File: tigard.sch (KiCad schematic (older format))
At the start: 87 parts, among them J1 USB_C_Receptacle_USB2.0, J2 JTAG, J3 UART, J4 SPI, J5 SWD, J6 I2C, Q1 BSH103, SW1 SW_DP4T, SW2 SW_DPDT, U1 AP7365-18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

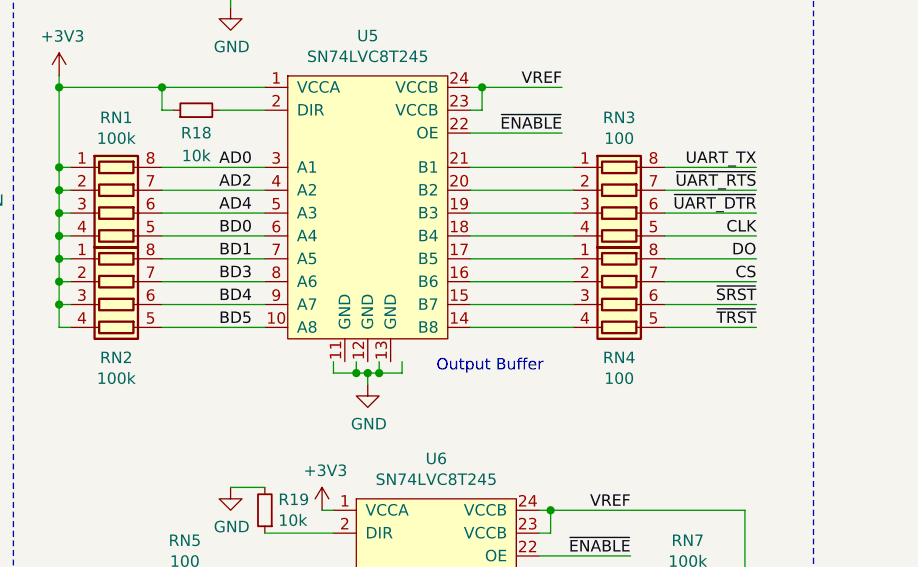
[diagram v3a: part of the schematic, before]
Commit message: Revise design to use cheaper TSSOP buffer footprint
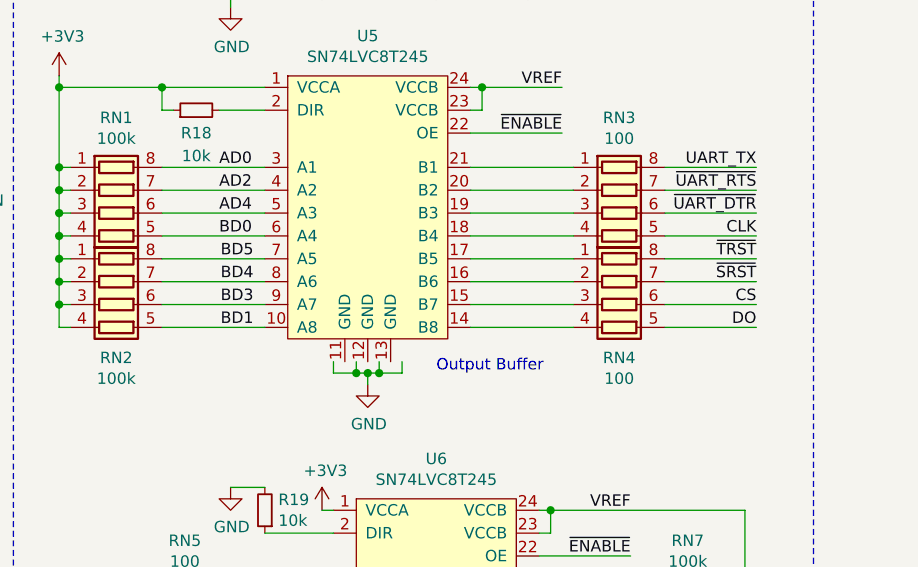
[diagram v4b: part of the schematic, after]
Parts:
- U5, U6: footprint tigard:Texas_VQFN-RHL-24_ThermalVias -> Package_SO:TSSOP-24_4.4x7.8mm_P0.65mm
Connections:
- net BD1: now also RN2.5 (R4.2), U5.10 (A8); no longer RN2.8 (R1.2), U5.7 (A5)
- net BD3: now also RN2.6 (R3.2), U5.9 (A7); no longer RN2.7 (R2.2), U5.8 (A6)
- net BD4: now also RN2.7 (R2.2), U5.8 (A6); no longer RN2.6 (R3.2), U5.9 (A7)
- net BD5: now also RN2.8 (R1.2), U5.7 (A5); no longer RN2.5 (R4.2), U5.10 (A8)
- net CS: now also RN4.6 (R3.2); no longer RN4.7 (R2.2)
- net DO: now also RN4.5 (R4.2); no longer RN4.8 (R1.2)
- net ~SRST: now also RN4.7 (R2.2); no longer RN4.6 (R3.2)
- net ~TRST: now also RN4.8 (R1.2); no longer RN4.5 (R4.2)
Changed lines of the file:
@@
 Wire Notes Line
 	4800 3050 4800 11150
-$Comp
-L tigard:SN74LVC8T245 U5
-U 1 1 5FA83347
-P 6350 5750
-F 0 "U5" H 6350 6625 50  0000 C CNN
-F 1 "SN74LVC8T245" H 6350 6534 50  0000 C CNN
-F 2 "tigard:Texas_VQFN-RHL-24_ThermalVias" H 6350 5850 50  0001 C CNN
-F 3 "" H 6350 5850 50  0001 C CNN
-F 4 "SN74LVC8T245RHLR" H 6350 5750 50  0001 C CNN "P/N"
-F 5 "C350563" H 6350 5750 50  0001 C CNN "LCSC"
-F 6 "ic-sn74lvc8t245" H 6350 5750 50  0001 C CNN "Key"
-	1    6350 5750
-	1    0    0    -1
-$EndComp
 Text Label 7200 5300 2    50   ~ 0
 ~ENABLE
@@
 Wire Wire Line
 	5450 5750 5900 5750
-Wire Wire Line
-	5450 5850 5900 5850
-Wire Wire Line
-	5450 5950 5900 5950
-Wire Wire Line
-	5450 6050 5900 6050
-Wire Wire Line
-	5450 6150 5900 6150
 $Comp
 L Device:R_Small R18
@@
 Wire Wire Line
 	5700 5200 5900 5200
-Text Label 5700 5450 0    50   ~ 0
-AD0
-Text Label 5700 5550 0    50   ~ 0
-AD2
-Text Label 5700 5650 0    50   ~ 0
-AD4
-Text Label 5700 5750 0    50   ~ 0
-BD0
-Text Label 5700 5850 0    50   ~ 0
-BD1
-Text Label 5700 5950 0    50   ~ 0
-BD3
-Text Label 5700 6050 0    50   ~ 0
-BD4
-Text Label 5700 6150 0    50   ~ 0
-BD5
-Text Label 8050 5450 2    50   ~ 0
-UART_TX
-Text Label 8050 5550 2    50   ~ 0
-~UART_RTS
-Text Label 8050 5650 2    50   ~ 0
-~UART_DTR
-Text Label 8050 5750 2    50   ~ 0
-CLK
-Text Label 8050 5850 2    50   ~ 0
-DO
-Text Label 8050 5950 2    50   ~ 0
-CS
-Text Label 8050 6050 2    50   ~ 0
-~SRST
-Text Label 8050 6150 2    50   ~ 0
-~TRST
-Wire Wire Line
-	8050 6150 7650 6150
-Wire Wire Line
-	7650 6050 8050 6050
-Wire Wire Line
-	8050 5950 7650 5950
-Wire Wire Line
-	7650 5850 8050 5850
-Wire Wire Line
-	8050 5750 7650 5750
-Wire Wire Line
-	7650 5650 8050 5650
-Wire Wire Line
-	8050 5550 7650 5550
-Wire Wire Line
-	7650 5450 8050 5450
 Wire Wire Line
 	7250 5450 6800 5450
@@
 Text Notes 6650 6350 0    50   ~ 0
 Output Buffer
-$Comp
-L tigard:SN74LVC8T245 U6
-U 1 1 601AD9F2
-P 6650 7600
-F 0 "U6" H 6650 8475 50  0000 C CNN
-F 1 "SN74LVC8T245" H 6650 8384 50  0000 C CNN
-F 2 "tigard:Texas_VQFN-RHL-24_ThermalVias" H 6650 7700 50  0001 C CNN
-F 3 "" H 6650 7700 50  0001 C CNN
-F 4 "SN74LVC8T245RHLR" H 6650 7600 50  0001 C CNN "P/N"
-F 5 "C350563" H 6650 7600 50  0001 C CNN "LCSC"
-F 6 "ic-sn74lvc8t245" H 6650 7600 50  0001 C CNN "Key"
-	1    6650 7600
-	1    0    0    -1
-$EndComp
 Text Label 7500 7150 2    50   ~ 0
 ~ENABLE
@@
 Wire Wire Line
 	7100 7150 7500 7150
-Wire Wire Line
-	5350 8000 5300 8000
-Wire Wire Line
-	5300 7800 5350 7800
-Wire Wire Line
-	5300 7900 5350 7900
 $Comp
 L Device:R_Small R19
@@
 Wire Wire Line
 	5750 8000 6200 8000
-Text Label 7500 7300 2    50   ~ 0
-UART_RX
-Text Label 7500 7400 2    50   ~ 0
-~UART_CTS
-Text Label 7500 7500 2    50   ~ 0
-~UART_DSR
-Text Label 7500 7600 2    50   ~ 0
-~UART_DCD
-Text Label 7500 7700 2    50   ~ 0
-DI
-NoConn ~ 5300 8000
-NoConn ~ 5300 7900
-NoConn ~ 5300 7800
-Text Label 5100 7300 0    50   ~ 0
-AD1
-Text Label 5100 7400 0    50   ~ 0
-AD3
-Text Label 5100 7500 0    50   ~ 0
-AD5
-Text Label 5100 7600 0    50   ~ 0
-AD6
-Text Label 5100 7700 0    50   ~ 0
-BD2
-Wire Wire Line
-	5100 7700 5350 7700
-Wire Wire Line
-	5100 7600 5350 7600
-Wire Wire Line
-	5100 7500 5350 7500
-Wire Wire Line
-	5100 7400 5350 7400
-Wire Wire Line
-	5100 7300 5350 7300
 Text Notes 7550 8650 0    100  Italic 20
 BUFFERS
@@
 	1    0    0    -1
 $EndComp
+Text Label 7500 7700 2    50   ~ 0
+DI
+Text Label 7500 7600 2    50   ~ 0
+~UART_DCD
+Text Label 7500 7500 2    50   ~ 0
+~UART_DSR
+Text Label 7500 7400 2    50   ~ 0
+~UART_CTS
+Text Label 7500 7300 2    50   ~ 0
+UART_RX
+Wire Wire Line
+	5100 7300 5350 7300
+Wire Wire Line
+	5100 7400 5350 7400
+Wire Wire Line
+	5100 7500 5350 7500
+Wire Wire Line
+	5100 7600 5350 7600
+Wire Wire Line
+	5100 7700 5350 7700
+Text Label 5100 7700 0    50   ~ 0
+BD2
+Text Label 5100 7600 0    50   ~ 0
+AD6
+Text Label 5100 7500 0    50   ~ 0
+AD5
+Text Label 5100 7400 0    50   ~ 0
+AD3
+Text Label 5100 7300 0    50   ~ 0
+AD1
+NoConn ~ 5300 7800
+NoConn ~ 5300 7900
+NoConn ~ 5300 8000
+Wire Wire Line
+	5300 7900 5350 7900
+Wire Wire Line
+	5300 7800 5350 7800
+Wire Wire Line
+	5350 8000 5300 8000
+Text Label 5700 5750 0    50   ~ 0
+BD0
+Text Label 5700 5650 0    50   ~ 0
+AD4
+Text Label 5700 5550 0    50   ~ 0
+AD2
+Text Label 5700 5450 0    50   ~ 0
+AD0
+Wire Wire Line
+	7650 5450 8050 5450
+Wire Wire Line
+	8050 5550 7650 5550
+Wire Wire Line
+	7650 5650 8050 5650
+Wire Wire Line
+	8050 5750 7650 5750
+Text Label 8050 5750 2    50   ~ 0
+CLK
+Text Label 8050 5650 2    50   ~ 0
+~UART_DTR
+Text Label 8050 5550 2    50   ~ 0
+~UART_RTS
+Text Label 8050 5450 2    50   ~ 0
+UART_TX
+Text Label 8050 6150 2    50   ~ 0
+DO
+Text Label 8050 6050 2    50   ~ 0
+CS
+Text Label 8050 5950 2    50   ~ 0
+~SRST
+Text Label 8050 5850 2    50   ~ 0
+~TRST
+$Comp
+L tigard:SN74LVC8T245 U5
+U 1 1 5FA83347
+P 6350 5750
+F 0 "U5" H 6350 6625 50  0000 C CNN
+F 1 "SN74LVC8T245" H 6350 6534 50  0000 C CNN
+F 2 "Package_SO:TSSOP-24_4.4x7.8mm_P0.65mm" H 6350 5850 50  0001 C CNN
+F 3 "" H 6350 5850 50  0001 C CNN
+F 4 "SN74LVC8T245RHLR" H 6350 5750 50  0001 C CNN "P/N"
+F 5 "C350563" H 6350 5750 50  0001 C CNN "LCSC"
+F 6 "ic-sn74lvc8t245" H 6350 5750 50  0001 C CNN "Key"
+	1    6350 5750
+	1    0    0    -1
+$EndComp
+$Comp
+L tigard:SN74LVC8T245 U6
+U 1 1 601AD9F2
+P 6650 7600
+F 0 "U6" H 6650 8475 50  0000 C CNN
+F 1 "SN74LVC8T245" H 6650 8384 50  0000 C CNN
+F 2 "Package_SO:TSSOP-24_4.4x7.8mm_P0.65mm" H 6650 7700 50  0001 C CNN
+F 3 "" H 6650 7700 50  0001 C CNN
+F 4 "SN74LVC8T245RHLR" H 6650 7600 50  0001 C CNN "P/N"
+F 5 "C350563" H 6650 7600 50  0001 C CNN "LCSC"
+F 6 "ic-sn74lvc8t245" H 6650 7600 50  0001 C CNN "Key"
+	1    6650 7600
+	1    0    0    -1
+$EndComp
+Text Label 5850 6150 2    50   ~ 0
+BD1
+Text Label 5850 6050 2    50   ~ 0
+BD3
+Text Label 5850 5950 2    50   ~ 0
+BD4
+Text Label 5850 5850 2    50   ~ 0
+BD5
+Wire Wire Line
+	5900 5850 5450 5850
+Wire Wire Line
+	5900 5950 5450 5950
+Wire Wire Line
+	5900 6050 5450 6050
+Wire Wire Line
+	5900 6150 5450 6150
+Wire Wire Line
+	8050 5850 7650 5850
+Wire Wire Line
+	7650 5950 8050 5950
+Wire Wire Line
+	8050 6050 7650 6050
+Wire Wire Line
+	7650 6150 8050 6150
 $EndSCHEMATC

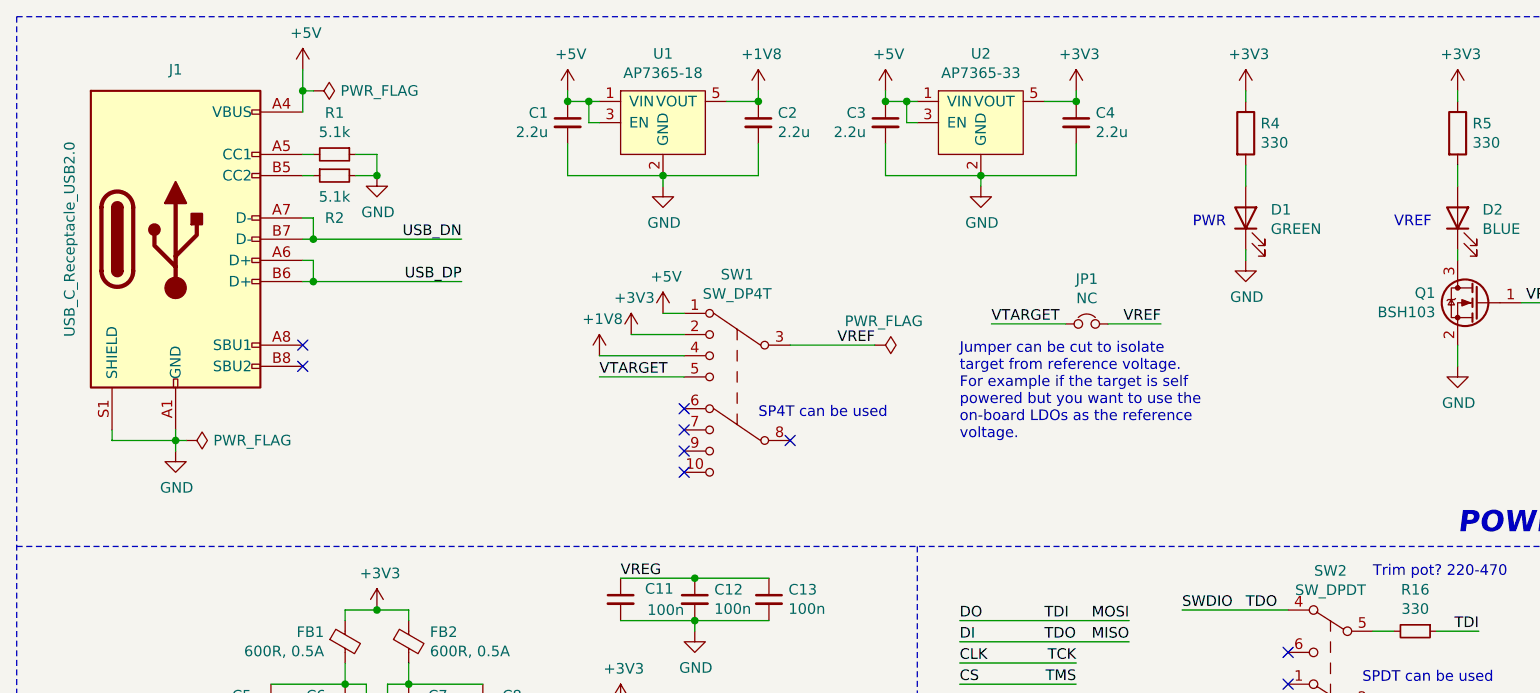
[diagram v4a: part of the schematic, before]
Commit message: Add USB filtering
* Ferrite and capacitor on VBUS per FTDI spec
* NF resistor and capacitor on shield to GND per FTDI spec
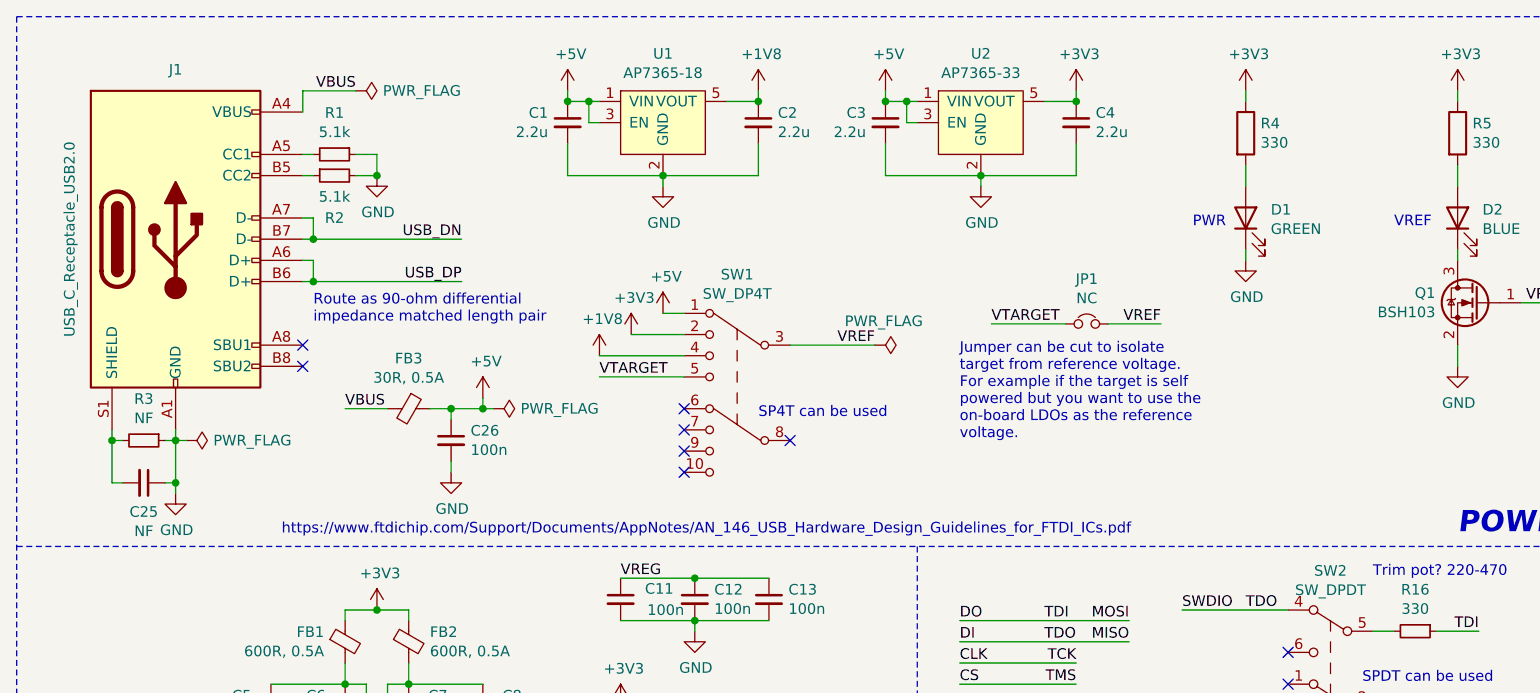
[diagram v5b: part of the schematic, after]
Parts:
- added C25: NF, Capacitor_SMD:C_0402_1005Metric, symbol Device:C_Small
- added C26: 100n, Capacitor_SMD:C_0402_1005Metric, symbol Device:C_Small
- added FB3: 30R, 0.5A, Inductor_SMD:L_0402_1005Metric, symbol Device:Ferrite_Bead_Small
- added R3: NF, Resistor_SMD:R_0402_1005Metric, symbol Device:R_Small
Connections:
- net +5V: now also C26.1, FB3.1; no longer J1.A4 (VBUS), J1.A9 (VBUS), J1.B4 (VBUS), J1.B9 (VBUS)
- net GND: now also C25.1, C26.2, R3.1; no longer J1.S1 (SHIELD)
- new net: C25.2, J1.S1 (SHIELD), R3.2
- new net VBUS: FB3.2, J1.A4 (VBUS), J1.A9 (VBUS), J1.B4 (VBUS), J1.B9 (VBUS)
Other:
- note added: "Route as 90-ohm differential\nimpedance matched length pair"
- note added: "https://www.ftdichip.com/Support/Documents/AppNotes/AN_146_USB_Hardware_Design_Guidelines_for_FTDI_ICs.pdf"
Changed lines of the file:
@@
 	1    0    0    -1
 $EndComp
-$Comp
-L power:+5V #PWR0101
-U 1 1 5EBD0634
-P 1900 800
-F 0 "#PWR0101" H 1900 650 50  0001 C CNN
-F 1 "+5V" H 1915 973 50  0000 C CNN
-F 2 "" H 1900 800 50  0001 C CNN
-F 3 "" H 1900 800 50  0001 C CNN
-	1    1900 800
-	1    0    0    -1
-$EndComp
-$Comp
-L power:PWR_FLAG #FLG0101
-U 1 1 5EBD0FDB
-P 1950 900
-F 0 "#FLG0101" H 1950 975 50  0001 C CNN
-F 1 "PWR_FLAG" V 1950 1028 50  0000 L CNN
-F 2 "" H 1950 900 50  0001 C CNN
-F 3 "~" H 1950 900 50  0001 C CNN
-	1    1950 900
-	0    1    1    0
-$EndComp
-Wire Wire Line
-	1950 900  1900 900
-Wire Wire Line
-	1900 900  1900 1000
-Wire Wire Line
-	1900 800  1900 900
-Connection ~ 1900 900
 NoConn ~ 1900 2100
 NoConn ~ 1900 2200
@@
 Connection ~ 2250 1300
 $Comp
-L power:GND #PWR0103
-U 1 1 5EBDCC81
-P 1300 2600
-F 0 "#PWR0103" H 1300 2350 50  0001 C CNN
-F 1 "GND" H 1305 2427 50  0000 C CNN
-F 2 "" H 1300 2600 50  0001 C CNN
-F 3 "" H 1300 2600 50  0001 C CNN
-	1    1300 2600
-	1    0    0    -1
-$EndComp
-Wire Wire Line
-	1300 2500 1300 2550
-Wire Wire Line
-	1000 2500 1000 2550
-Wire Wire Line
-	1000 2550 1300 2550
-Connection ~ 1300 2550
-Wire Wire Line
-	1300 2550 1300 2600
-$Comp
 L tigard:AP7365-18 U1
 U 1 1 5EBDE10A
@@
 	7350 1250 7350 1350
 $Comp
-L power:PWR_FLAG #FLG0102
-U 1 1 5EC75448
-P 1350 2550
-F 0 "#FLG0102" H 1350 2625 50  0001 C CNN
-F 1 "PWR_FLAG" V 1350 2678 50  0000 L CNN
-F 2 "" H 1350 2550 50  0001 C CNN
-F 3 "~" H 1350 2550 50  0001 C CNN
-	1    1350 2550
-	0    1    1    0
-$EndComp
-Wire Wire Line
-	1300 2550 1350 2550
-$Comp
 L power:+3V3 #PWR0116
 U 1 1 5EC79112
@@
 Wire Wire Line
 	7650 6150 8050 6150
+$Comp
+L Device:R_Small R3
+U 1 1 5F3A89C1
+P 1150 2550
+F 0 "R3" V 954 2550 50  0000 C CNN
+F 1 "NF" V 1045 2550 50  0000 C CNN
+F 2 "Resistor_SMD:R_0402_1005Metric" H 1150 2550 50  0001 C CNN
+F 3 "~" H 1150 2550 50  0001 C CNN
+	1    1150 2550
+	0    1    1    0
+$EndComp
+Wire Wire Line
+	1300 2550 1350 2550
+$Comp
+L power:PWR_FLAG #FLG0102
+U 1 1 5EC75448
+P 1350 2550
+F 0 "#FLG0102" H 1350 2625 50  0001 C CNN
+F 1 "PWR_FLAG" V 1350 2678 50  0000 L CNN
+F 2 "" H 1350 2550 50  0001 C CNN
+F 3 "~" H 1350 2550 50  0001 C CNN
+	1    1350 2550
+	0    1    1    0
+$EndComp
+Connection ~ 1300 2550
+Wire Wire Line
+	1300 2500 1300 2550
+$Comp
+L Device:C_Small C25
+U 1 1 5F3A982F
+P 1150 2750
+F 0 "C25" V 1287 2750 50  0000 C CNN
+F 1 "NF" V 1378 2750 50  0000 C CNN
+F 2 "Capacitor_SMD:C_0402_1005Metric" H 1150 2750 50  0001 C CNN
+F 3 "~" H 1150 2750 50  0001 C CNN
+	1    1150 2750
+	0    1    1    0
+$EndComp
+$Comp
+L power:GND #PWR0103
+U 1 1 5EBDCC81
+P 1300 2800
+F 0 "#PWR0103" H 1300 2550 50  0001 C CNN
+F 1 "GND" H 1305 2627 50  0000 C CNN
+F 2 "" H 1300 2800 50  0001 C CNN
+F 3 "" H 1300 2800 50  0001 C CNN
+	1    1300 2800
+	1    0    0    -1
+$EndComp
+Wire Wire Line
+	1000 2500 1000 2550
+Wire Wire Line
+	1050 2550 1000 2550
+Connection ~ 1000 2550
+Wire Wire Line
+	1000 2550 1000 2750
+Wire Wire Line
+	1250 2550 1300 2550
+Wire Wire Line
+	1000 2750 1050 2750
+Wire Wire Line
+	1300 2550 1300 2750
+Wire Wire Line
+	1250 2750 1300 2750
+Wire Wire Line
+	1300 2800 1300 2750
+Connection ~ 1300 2750
+$Comp
+L power:PWR_FLAG #FLG0101
+U 1 1 5EBD0FDB
+P 2800 2400
+F 0 "#FLG0101" H 2800 2475 50  0001 C CNN
+F 1 "PWR_FLAG" V 2800 2528 50  0000 L CNN
+F 2 "" H 2800 2400 50  0001 C CNN
+F 3 "~" H 2800 2400 50  0001 C CNN
+	1    2800 2400
+	0    1    1    0
+$EndComp
+$Comp
+L Device:Ferrite_Bead_Small FB3
+U 1 1 5FA24965
+P 2400 2400
+F 0 "FB3" V 2163 2400 50  0000 C CNN
+F 1 "30R, 0.5A" V 2254 2400 50  0000 C CNN
+F 2 "Inductor_SMD:L_0402_1005Metric" V 2330 2400 50  0001 C CNN
+F 3 "~" H 2400 2400 50  0001 C CNN
+F 4 "SBY100505T-300Y-N" V 2400 2400 50  0001 C CNN "P/N"
+F 5 "C142032" V 2400 2400 50  0001 C CNN "LCSC"
+F 6 "ferrite-0402-30" V 2400 2400 50  0001 C CNN "Key"
+	1    2400 2400
+	0    1    1    0
+$EndComp
+$Comp
+L Device:C_Small C26
+U 1 1 5FA89FD4
+P 2600 2550
+F 0 "C26" H 2692 2596 50  0000 L CNN
+F 1 "100n" H 2692 2505 50  0000 L CNN
+F 2 "Capacitor_SMD:C_0402_1005Metric" H 2600 2550 50  0001 C CNN
+F 3 "~" H 2600 2550 50  0001 C CNN
+F 4 "CL05A104KA5NNNC" H 2600 2550 50  0001 C CNN "P/N"
+F 5 "C100072" H 2600 2550 50  0001 C CNN "LCSC"
+F 6 "cap-cer-0402-100n" H 2600 2550 50  0001 C CNN "Key"
+	1    2600 2550
+	1    0    0    -1
+$EndComp
+$Comp
+L power:+5V #PWR02
+U 1 1 5FC89889
+P 2750 2350
+F 0 "#PWR02" H 2750 2200 50  0001 C CNN
+F 1 "+5V" H 2765 2523 50  0000 C CNN
+F 2 "" H 2750 2350 50  0001 C CNN
+F 3 "" H 2750 2350 50  0001 C CNN
+	1    2750 2350
+	1    0    0    -1
+$EndComp
+Wire Wire Line
+	2750 2350 2750 2400
+Connection ~ 2750 2400
+Wire Wire Line
+	2750 2400 2800 2400
+Text Notes 1800 3000 0    50   ~ 0
+https://www.ftdichip.com/Support/Documents/AppNotes/AN_146_USB_Hardware_Design_Guidelines_for_FTDI_ICs.pdf
+Text Notes 1950 2000 0    50   ~ 0
+Route as 90-ohm differential\nimpedance matched length pair
+$Comp
+L power:PWR_FLAG #FLG0105
+U 1 1 5FF4F762
+P 2150 900
+F 0 "#FLG0105" H 2150 975 50  0001 C CNN
+F 1 "PWR_FLAG" V 2150 1028 50  0000 L CNN
+F 2 "" H 2150 900 50  0001 C CNN
+F 3 "~" H 2150 900 50  0001 C CNN
+	1    2150 900
+	0    1    1    0
+$EndComp
+Text Label 2150 900  2    50   ~ 0
+VBUS
+Wire Wire Line
+	2150 900  1900 900
+Wire Wire Line
+	1900 900  1900 1000
+Text Label 2100 2400 0    50   ~ 0
+VBUS
+Wire Wire Line
+	2100 2400 2300 2400
+$Comp
+L power:GND #PWR0101
+U 1 1 602C545A
+P 2600 2700
+F 0 "#PWR0101" H 2600 2450 50  0001 C CNN
+F 1 "GND" H 2605 2527 50  0000 C CNN
+F 2 "" H 2600 2700 50  0001 C CNN
+F 3 "" H 2600 2700 50  0001 C CNN
+	1    2600 2700
+	1    0    0    -1
+$EndComp
+Wire Wire Line
+	2500 2400 2600 2400
+Wire Wire Line
+	2600 2400 2600 2450
+Connection ~ 2600 2400
+Wire Wire Line
+	2600 2400 2750 2400
+Wire Wire Line
+	2600 2650 2600 2700
 $EndSCHEMATC
